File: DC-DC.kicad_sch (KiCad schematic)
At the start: 23 parts, among them U4 LD39200PU33R, U6 TPS62933

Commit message: 3/8/2025
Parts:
- added C36: 10 uF, Capacitor_SMD:C_1210_3225Metric, symbol Device:C
- added C37: 100 nF, Capacitor_SMD:C_0603_1608Metric, symbol Device:C
- added C38: 47 pF, Capacitor_SMD:C_0603_1608Metric, symbol Device:C
- added C39, C42: 22 uF, Capacitor_SMD:C_1206_3216Metric, symbol Device:C
- added C40, C41: 1 uF, Capacitor_SMD:C_0603_1608Metric, symbol Device:C
- added J13, J14, J16: Conn_02x02_Counter_Clockwise, Connector_PinHeader_2.54mm:PinHeader_2x02_P2.54mm_Vertical, symbol Connector_Generic:Conn_02x02_Counter_Clockwise
- added L2: 6.8 uH, jka_library:SRP6060FA5R6M, symbol Device:L
- added R36, R37: 10k, Resistor_SMD:R_0603_1608Metric, symbol Device:R_US
- added R38: 158k, Resistor_SMD:R_0603_1608Metric, symbol Device:R_US
- added R39: 30.1k, Resistor_SMD:R_0603_1608Metric, symbol Device:R_US
- added U8: AP63300WU-7, jka_library:TSOT6_AP63300WU-7_DIO, symbol jka_library:AP63300WU-7
- added U9: LDL112PV18R, jka_library:DFN6_3P1X3P1X0P95_STM, symbol jka_library:LDL112PV18R
- C25: renamed from C18; footprint (none) -> Capacitor_SMD:C_1210_3225Metric
- C26: renamed from C?; footprint (none) -> Capacitor_SMD:C_0603_1608Metric
- C27: renamed from C16; footprint (none) -> Capacitor_SMD:C_1210_3225Metric
- C28: renamed from C13; footprint (none) -> Capacitor_SMD:C_0805_2012Metric
- C29: renamed from C17; footprint (none) -> Capacitor_SMD:C_0603_1608Metric
- C30: renamed from C19; footprint (none) -> Capacitor_SMD:C_0603_1608Metric
- C31: renamed from C15; footprint (none) -> Capacitor_SMD:C_0603_1608Metric
- C32: renamed from C20; footprint (none) -> Capacitor_SMD:C_1210_3225Metric
- C33: renamed from C14; footprint (none) -> Capacitor_SMD:C_0805_2012Metric
- C34: renamed from C21; footprint (none) -> Capacitor_SMD:C_1210_3225Metric
- C35: renamed from C22; footprint (none) -> Capacitor_SMD:C_0603_1608Metric
- D10: renamed from D7; footprint (none) -> Diode_SMD:D_0603_1608Metric
- D9: renamed from D8; footprint (none) -> Diode_SMD:D_0603_1608Metric
- L1: renamed from L2; footprint (none) -> jka_library:SRP6060FA5R6M
- R29: renamed from R23; footprint (none) -> Resistor_SMD:R_0603_1608Metric
- R30: renamed from R24; footprint (none) -> Resistor_SMD:R_0603_1608Metric
- R31: renamed from R22; value 1 -> 1R; footprint (none) -> Resistor_SMD:R_0603_1608Metric
- R32: renamed from R25; footprint (none) -> Resistor_SMD:R_0603_1608Metric
- R33: renamed from R26; footprint (none) -> Resistor_SMD:R_0603_1608Metric
- R34: renamed from R20; value 0 -> 0R; footprint (none) -> Resistor_SMD:R_0603_1608Metric
- R35: renamed from R2; footprint (none) -> Resistor_SMD:R_0603_1608Metric
- renumbered U4 to U6, U6 to U7
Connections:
- net GND: now also C36.2, C39.2, C40.2, C41.1, C42.2, J13.1 (Pin_1), J13.2 (Pin_2), J14.1 (Pin_1), J14.2 (Pin_2), J16.1 (Pin_1), J16.2 (Pin_2), R39.1, U8.4 (GND), U9.2 (GND), U9.7 (EPAD)
- net VIN: now also C36.1, R36.1, U8.3 (VIN)
- net +3.3V renamed +3V3
- net +3V3: now also J13.3 (Pin_3), J13.4 (Pin_4)
- new net: C38.2, R38.1, R39.2, U8.1 (FB)
- new net: C37.2, L2.1, U8.5 (SW)
- new net: C37.1, U8.6 (BST)
- new net +1V8: C40.1, J14.3 (Pin_3), J14.4 (Pin_4), U9.4 (VOUT)
- new net +1V8_EN: R37.2, U9.1 (EN)
- new net +5V: C38.1, C39.1, C41.2, C42.1, J16.3 (Pin_3), J16.4 (Pin_4), L2.2, R37.1, R38.2, U9.6 (VIN)
- new net +5V_EN: R36.2, U8.2 (EN)
- no-connect marks 0 -> 1
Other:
- note added: "1.8V Rail"
- note added: "3.3V Rail"
- note added: "5V Bus"
- note added: "Floating EN enables device"
- note added: "Main Bus (3.6V)"
- note added: "SS Cap 6.8 nF min"
- note removed: "6.8 nF min"
- note removed: "DC-DC for Main Bus"
- moved on the sheet: C25, C26, C27, C28, C29, C30, C31, C32, C33, C34, C35, D10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

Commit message: Layout draft complete
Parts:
- removed D9: LED, Diode_SMD:D_0603_1608Metric, symbol Device:LED
- added D12: LED, Diode_SMD:D_0603_1608Metric, symbol Device:LED
- added R41, R44: 1k, Resistor_SMD:R_0603_1608Metric, symbol Device:R_US
- J16: value Conn_02x02_Counter_Clockwise -> Conn_02x02
- R29: value R -> 0R; now fitted
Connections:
- net +3V3: now also D12.2 (A), R41.1; no longer R29.2
- net +5V: no longer R37.1
- net GND: now also R29.1, R36.1, R37.1, R44.2; no longer C26.2
- net 5V_BUCK_SW: now reaches C37.2, L2.1, U8.5 (SW)
- net BUCK_OUT renamed 3V6_BUCK_OUT
- net VIN renamed VBUS_MAIN
- net VBUS_MAIN: no longer R36.1
- new net: D12.1 (K), R44.1
- new net: C26.2, R29.2, R41.2
- no-connect marks 1 -> 2
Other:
- note added: "If 32/32/33F variant, place cap and resistor If 33P/33O, place diode and resistor"
- note added: "VBUS MAIN can range from 4.8V to 22.8V from USB PD"
- note removed: "Inputs"
- note removed: "Outputs"
- note removed: "VIN can range from 4.8V to 22.8V from USB PD"
- title: (none) -> Jakka1
- moved on the sheet: C26, C28, C33, C37, D10, J13, J16, R35, R37, U6

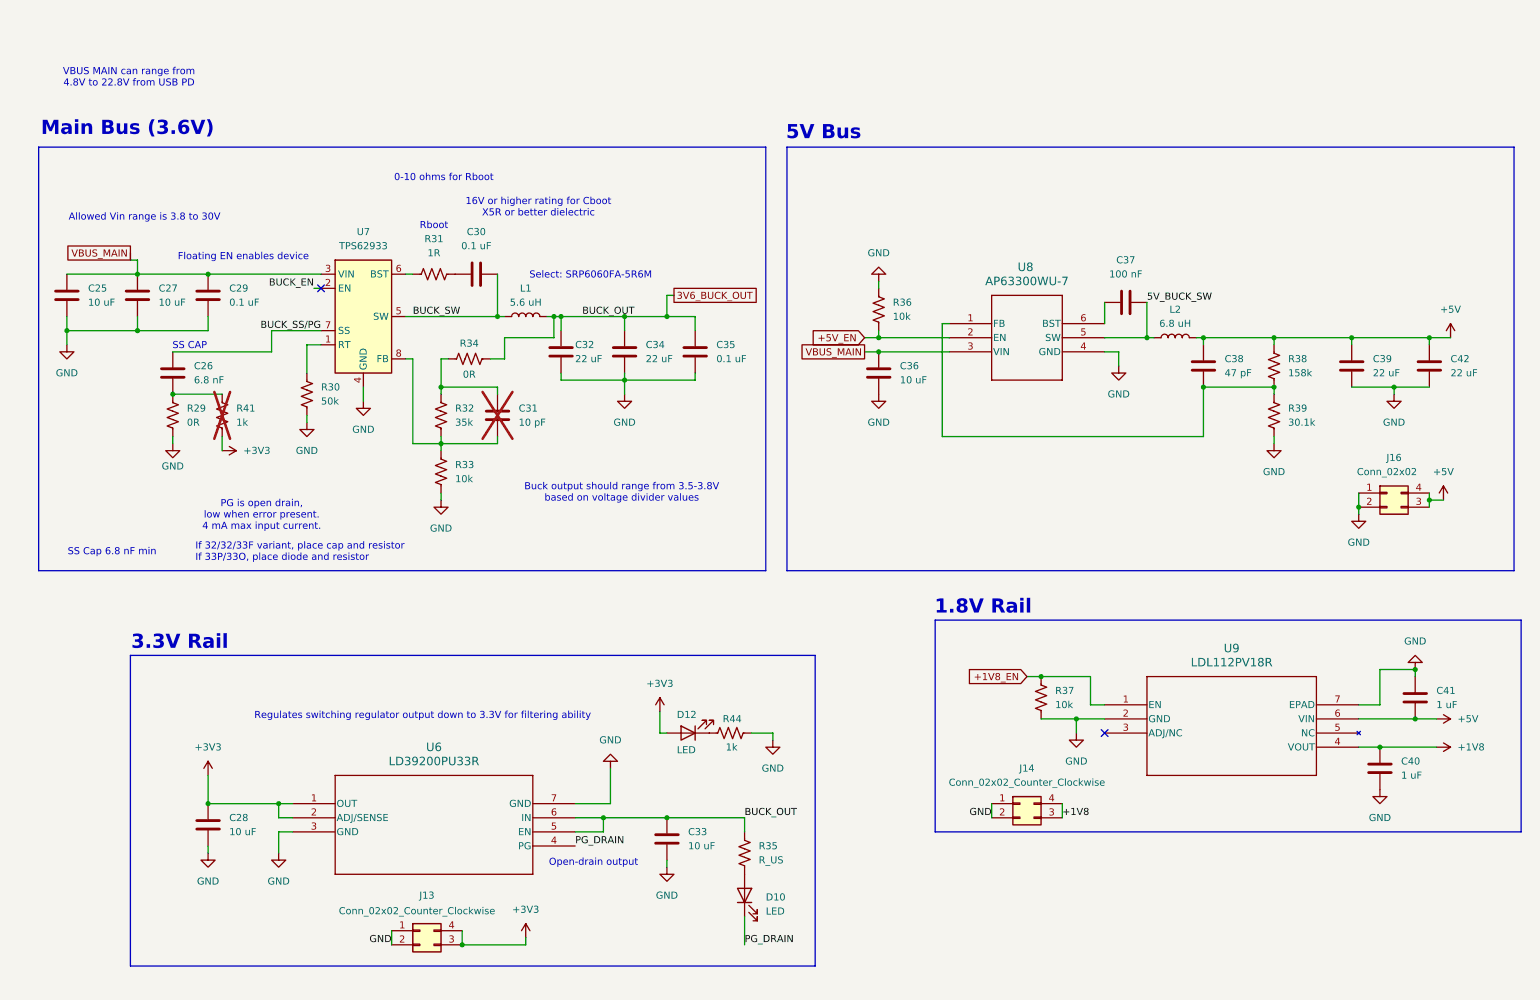
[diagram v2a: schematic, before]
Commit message: First draft of design output, schematic, and layout complete
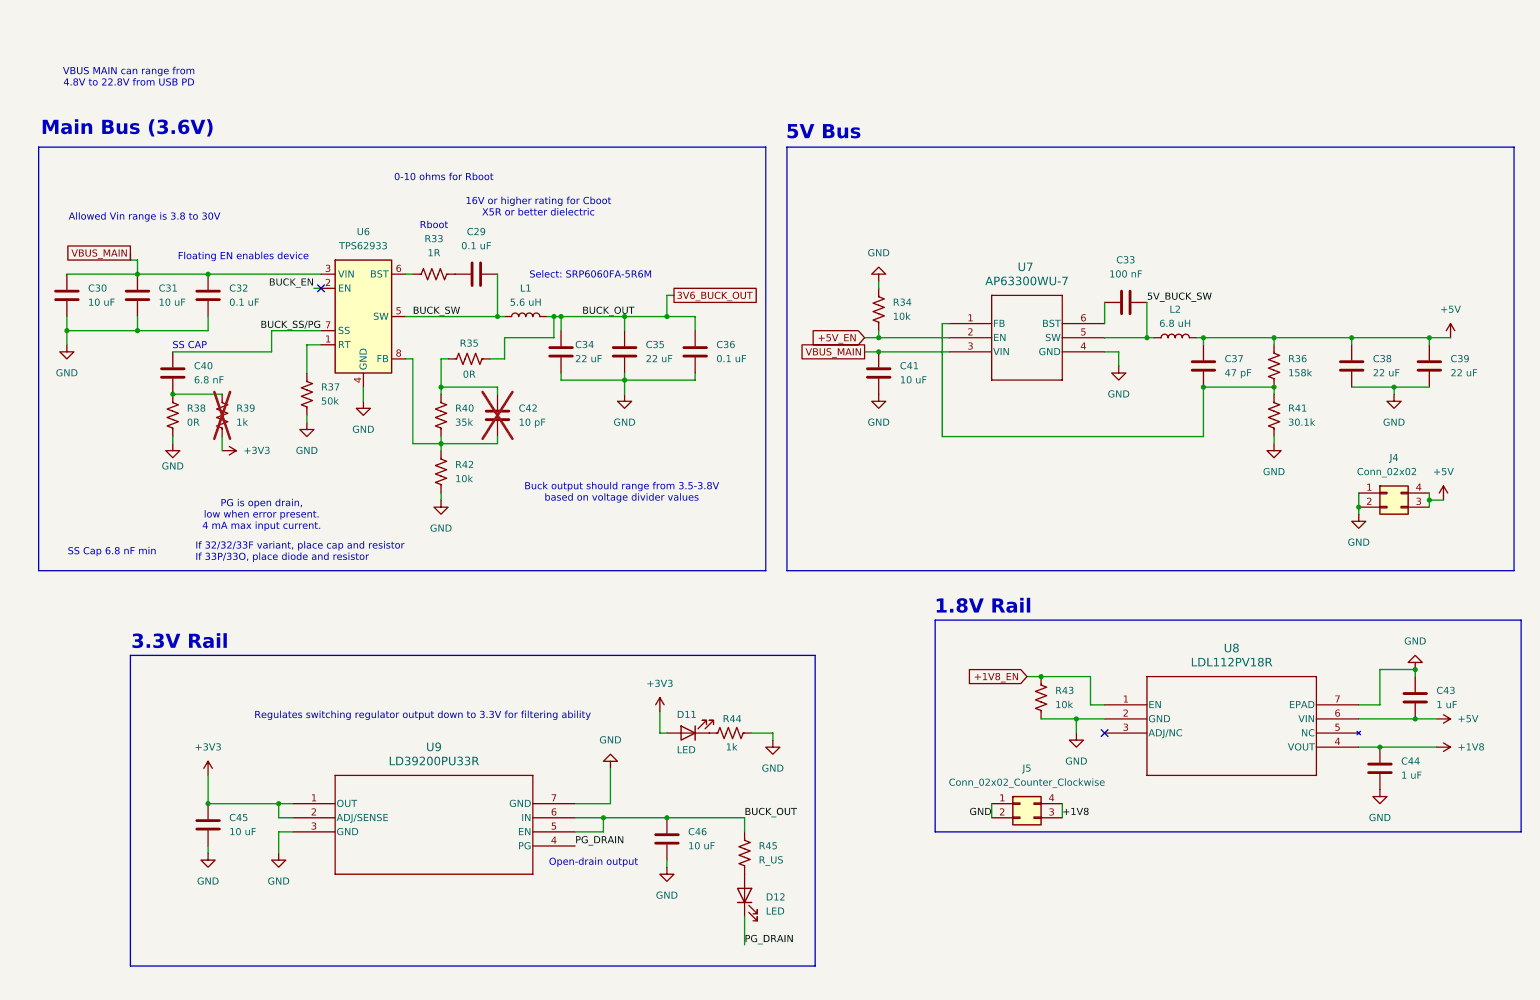
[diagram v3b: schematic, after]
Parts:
- removed J13: Conn_02x02_Counter_Clockwise, Connector_PinHeader_2.54mm:PinHeader_2x02_P2.54mm_Vertical, symbol Connector_Generic:Conn_02x02_Counter_Clockwise
- renumbered C30 to C29, C25 to C30, C27 to C31, C29 to C32, C37 to C33, C32 to C34, C34 to C35, C35 to C36, C38 to C37, C39 to C38, C42 to C39, C26 to C40, C36 to C41, C31 to C42, C41 to C43, C40 to C44, C28 to C45, C33 to C46, D12 to D11, D10 to D12, J16 to J4, J14 to J5, R31 to R33, R36 to R34, R34 to R35, R38 to R36, R30 to R37, R29 to R38, R41 to R39, R32 to R40, R39 to R41, R33 to R42, R37 to R43, R35 to R45, U7 to U6, U8 to U7, U9 to U8, U6 to U9
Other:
- company: (none) -> Jacob Kapala
